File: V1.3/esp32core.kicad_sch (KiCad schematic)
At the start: 1 part, among them U1 ESP32-DEVKITC-32D

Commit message: update v1.3 schematic documentation
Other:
- note added: "ESP32 DevKitC v4+"
- note added: "This shows a component to represent the ESP32-DEVKITC-V4+ board, as it will be seated in place. However, the component itself is not included on the circuit board, instead seating into some breakout headers for easy replacement. This page is for reference only, not design."
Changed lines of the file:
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@@
     (effects (font (size 1.27 1.27)) (justify left bottom))
+  )
+  (text "ESP32 DevKitC v4+" (at 71.12 53.34 0)
+    (effects (font (size 10 10) (thickness 0.7) bold italic) (justify left bottom))
   )
   (text "Do Not Use" (at 189.23 114.3 0)
@@
     (effects (font (size 1.27 1.27)) (justify right bottom))
   )
+  (text "This shows a component to represent the \nESP32-DEVKITC-V4+ board, as it will be \nseated in place. However, the component \nitself is not included on the circuit \nboard, instead seating into some breakout \nheaders for easy replacement. This page \nis for reference only, not design."
+    (at 25.4 186.69 0)
+    (effects (font (size 3.5 3.5)) (justify left bottom))
+  )
   (text "Do Not Use" (at 189.23 124.46 0)

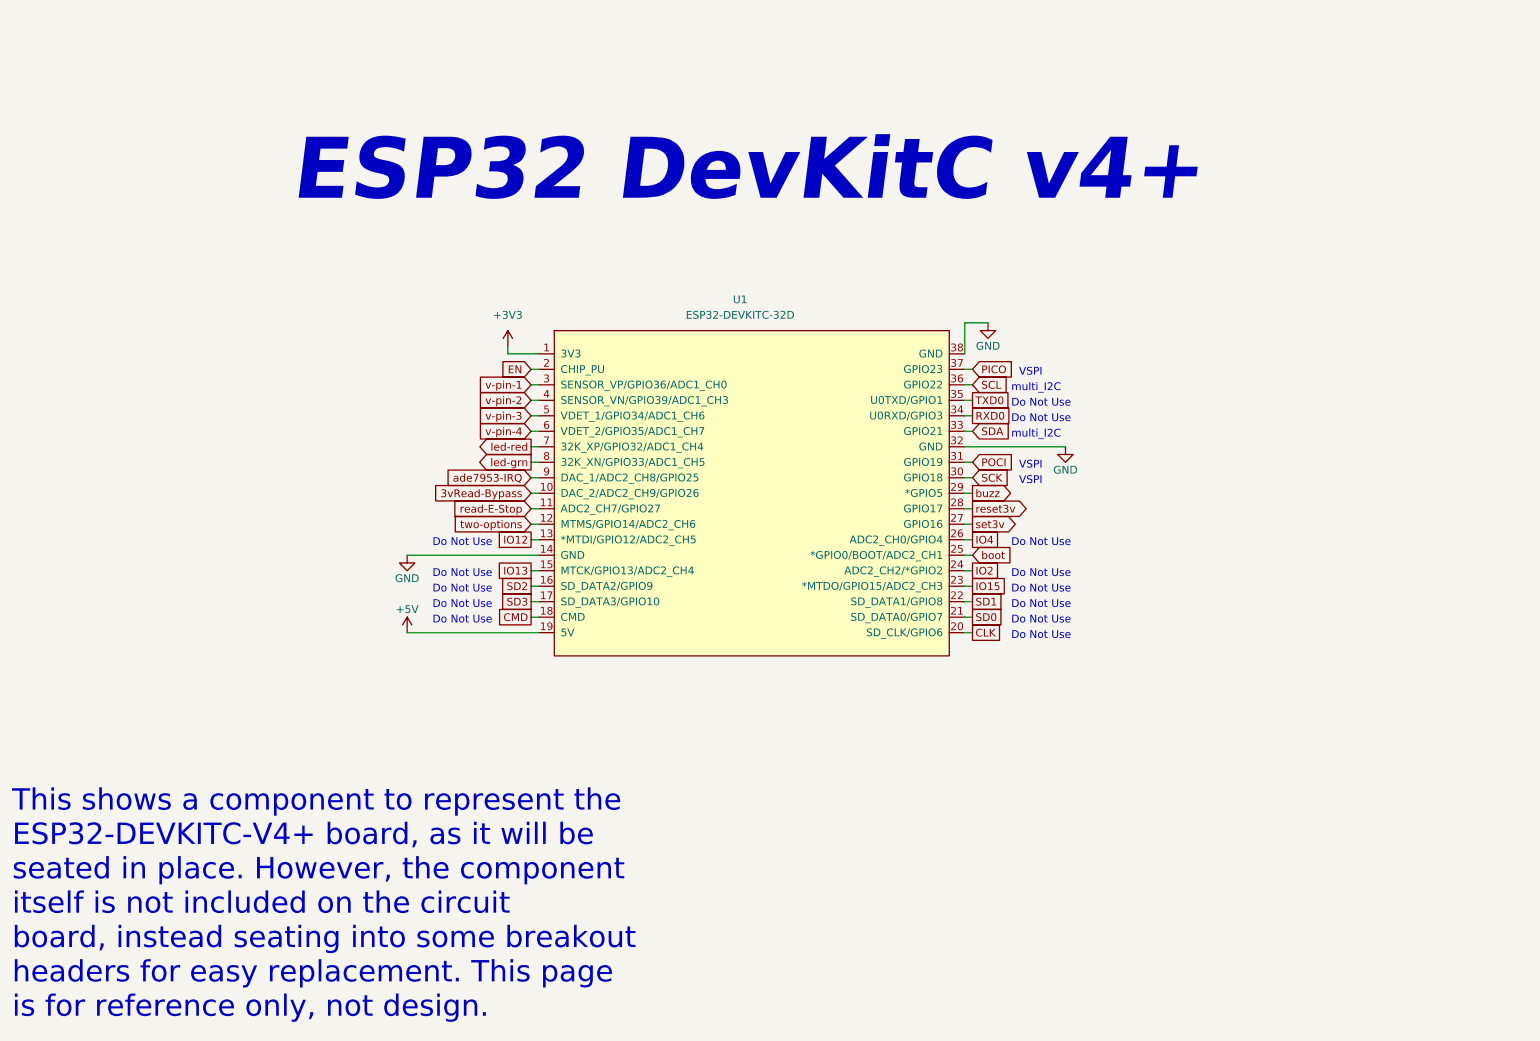
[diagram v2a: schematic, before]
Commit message: started adding the feather footprint to the board. need to update board shape and silkscreens
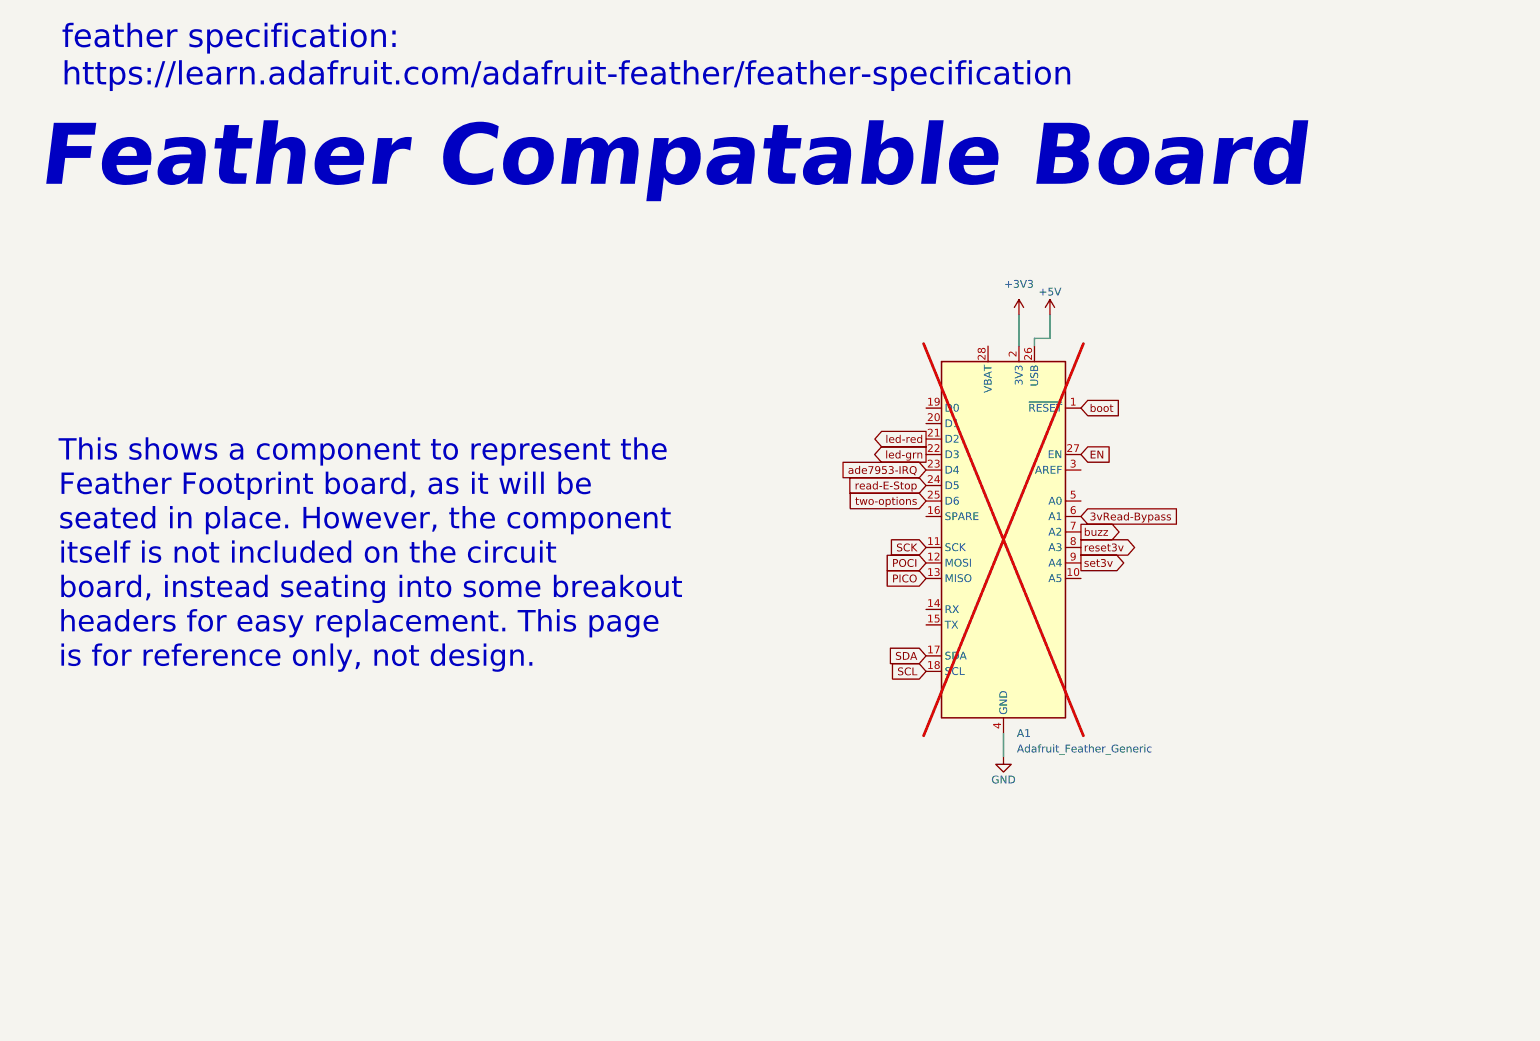
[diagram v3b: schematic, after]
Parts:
- removed U1: ESP32-DEVKITC-32D, Espressif:ESP32-DevKitC, symbol espressif:ESP32-DevKitC
- added A1: Adafruit_Feather_Generic, Module:Adafruit_Feather, symbol MCU_Module:Adafruit_Feather_Generic
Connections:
- net +3V3: now also A1.2 (3V3)
- net +5V: now also A1.26 (USB)
- net 3vRead-Bypass: now also A1.6 (A1)
- net EN: now also A1.27 (EN)
- net GND: now also A1.4 (GND)
- net PICO: now also A1.13 (MISO)
- net POCI: now also A1.12 (MOSI)
- net SCK: now also A1.11 (SCK)
- net SCL: now also A1.18 (SCL)
- net SDA: now also A1.17 (SDA)
- net ade7953-IRQ: now also A1.23 (D4)
- net boot: now also A1.1 (~{RESET})
- net buzz: now also A1.7 (A2)
- net led-grn: now also A1.22 (D3)
- net led-red: now also A1.21 (D2)
- net read-E-Stop: now also A1.24 (D5)
- net reset3v: now also A1.8 (A3)
- net set3v: now also A1.9 (A4)
- net two-options: now also A1.25 (D6)
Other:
- note added: "Feather Compatable Board"
- note added: "This shows a component to represent the Feather Footprint board, as it will be seated in place. However, the component itself is not included on the circuit board, instead seating into some breakout headers for easy replacement. This page is for reference only, not design."
- note added: "feather specification: https://learn.adafruit.com/adafruit-feather/feather-specification"
- note removed: "Do Not Use"
- note removed: "ESP32 DevKitC v4+"
- note removed: "This shows a component to represent the ESP32-DEVKITC-V4+ board, as it will be seated in place. However, the component itself is not included on the circuit board, instead seating into some breakout headers for easy replacement. This page is for reference only, not design."
- note removed: "VSPI"
- note removed: "multi_I2C"

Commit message: design for feather-based board should work, but nothing is pretty
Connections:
- net 3vRead-Bypass: no longer A1.6 (A1)
- net ade7953-IRQ: no longer A1.23 (D4)
- net buzz: no longer A1.7 (A2)
- net led-grn: no longer A1.22 (D3)
- net led-red: no longer A1.21 (D2)
- net read-E-Stop: no longer A1.24 (D5)
- net reset3v: no longer A1.8 (A3)
- net set3v: no longer A1.9 (A4)
- net two-options: no longer A1.25 (D6)
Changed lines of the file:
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@@
 	(global_label "led-red"
 		(shape output)
-		(at 175.26 91.44 180)
-		(fields_autoplaced yes)
-		(effects
-			(font
-				(size 1.27 1.27)
-			)
-			(justify right)
-		)
-		(property "Intersheetrefs" "${INTERSHEET_REFS}"
-			(at 165.3479 91.3606 0)
+		(at 166.37 91.44 180)
+		(fields_autoplaced yes)
+		(effects
+			(font
+				(size 1.27 1.27)
+			)
+			(justify right)
+		)
+		(property "Intersheetrefs" "${INTERSHEET_REFS}"
+			(at 156.4579 91.3606 0)
 			(effects
 				(font
@@
 	(global_label "two-options"
 		(shape input)
-		(at 175.26 101.6 180)
-		(fields_autoplaced yes)
-		(effects
-			(font
-				(size 1.27 1.27)
-			)
-			(justify right)
-		)
-		(property "Intersheetrefs" "${INTERSHEET_REFS}"
-			(at 161.1145 101.5206 0)
+		(at 166.37 101.6 180)
+		(fields_autoplaced yes)
+		(effects
+			(font
+				(size 1.27 1.27)
+			)
+			(justify right)
+		)
+		(property "Intersheetrefs" "${INTERSHEET_REFS}"
+			(at 152.2245 101.5206 0)
 			(effects
 				(font
@@
 	(global_label "ade7953-IRQ"
 		(shape input)
-		(at 175.26 96.52 180)
-		(fields_autoplaced yes)
-		(effects
-			(font
-				(size 1.27 1.27)
-			)
-			(justify right)
-		)
-		(property "Intersheetrefs" "${INTERSHEET_REFS}"
-			(at 159.8445 96.4406 0)
+		(at 166.37 96.52 180)
+		(fields_autoplaced yes)
+		(effects
+			(font
+				(size 1.27 1.27)
+			)
+			(justify right)
+		)
+		(property "Intersheetrefs" "${INTERSHEET_REFS}"
+			(at 150.9545 96.4406 0)
 			(effects
 				(font
@@
 	(global_label "led-grn"
 		(shape output)
-		(at 175.26 93.98 180)
-		(fields_autoplaced yes)
-		(effects
-			(font
-				(size 1.27 1.27)
-			)
-			(justify right)
-		)
-		(property "Intersheetrefs" "${INTERSHEET_REFS}"
-			(at 165.2874 93.9006 0)
+		(at 166.37 93.98 180)
+		(fields_autoplaced yes)
+		(effects
+			(font
+				(size 1.27 1.27)
+			)
+			(justify right)
+		)
+		(property "Intersheetrefs" "${INTERSHEET_REFS}"
+			(at 156.3974 93.9006 0)
 			(effects
 				(font
@@
 	(global_label "reset3v"
 		(shape output)
-		(at 200.66 109.22 0)
-		(fields_autoplaced yes)
-		(effects
-			(font
-				(size 1.27 1.27)
-			)
-			(justify left)
-		)
-		(property "Intersheetrefs" "${INTERSHEET_REFS}"
-			(at 209.9674 109.2994 0)
+		(at 209.55 109.22 0)
+		(fields_autoplaced yes)
+		(effects
+			(font
+				(size 1.27 1.27)
+			)
+			(justify left)
+		)
+		(property "Intersheetrefs" "${INTERSHEET_REFS}"
+			(at 218.8574 109.2994 0)
 			(effects
 				(font
@@
 	(global_label "read-E-Stop"
 		(shape input)
-		(at 175.26 99.06 180)
-		(fields_autoplaced yes)
-		(effects
-			(font
-				(size 1.27 1.27)
-			)
-			(justify right)
-		)
-		(property "Intersheetrefs" "${INTERSHEET_REFS}"
-			(at 160.1469 98.9806 0)
+		(at 166.37 99.06 180)
+		(fields_autoplaced yes)
+		(effects
+			(font
+				(size 1.27 1.27)
+			)
+			(justify right)
+		)
+		(property "Intersheetrefs" "${INTERSHEET_REFS}"
+			(at 151.2569 98.9806 0)
 			(effects
 				(font
@@
 	(global_label "buzz"
 		(shape output)
-		(at 200.66 106.68 0)
-		(fields_autoplaced yes)
-		(effects
-			(font
-				(size 1.27 1.27)
-			)
-			(justify left)
-		)
-		(property "Intersheetrefs" "${INTERSHEET_REFS}"
-			(at 207.4274 106.6006 0)
+		(at 209.55 106.68 0)
+		(fields_autoplaced yes)
+		(effects
+			(font
+				(size 1.27 1.27)
+			)
+			(justify left)
+		)
+		(property "Intersheetrefs" "${INTERSHEET_REFS}"
+			(at 216.3174 106.6006 0)
 			(effects
 				(font
@@
 	(global_label "set3v"
 		(shape output)
-		(at 200.66 111.76 0)
-		(fields_autoplaced yes)
-		(effects
-			(font
-				(size 1.27 1.27)
-			)
-			(justify left)
-		)
-		(property "Intersheetrefs" "${INTERSHEET_REFS}"
-			(at 208.0926 111.6806 0)
+		(at 209.55 111.76 0)
+		(fields_autoplaced yes)
+		(effects
+			(font
+				(size 1.27 1.27)
+			)
+			(justify left)
+		)
+		(property "Intersheetrefs" "${INTERSHEET_REFS}"
+			(at 216.9826 111.6806 0)
 			(effects
 				(font
@@
 	(global_label "3vRead-Bypass"
 		(shape input)
-		(at 200.66 104.14 0)
-		(fields_autoplaced yes)
-		(effects
-			(font
-				(size 1.27 1.27)
-			)
-			(justify left)
-		)
-		(property "Intersheetrefs" "${INTERSHEET_REFS}"
-			(at 218.6431 104.14 0)
-			(effects
-				(font
+		(at 209.55 104.14 0)
+		(fields_autoplaced yes)
+		(effects
+			(font
+				(size 1.27 1.27)
+			)
+			(justify left)
+		)
+		(property "Intersheetrefs" "${INTERSHEET_REFS}"
+			(at 227.5331 104.14 0)
+			(effects
+				(font
